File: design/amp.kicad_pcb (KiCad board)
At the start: 2 copper layers, 61 x 36 mm, 57 parts, among them IC1 CP2102N-A02-GQFN24R, IC2 STM6601CQ2BDM6F, IC3 LD39200PU33R, J1 USB4105-GF-A, J2 SM04B-SRSS-TB(LF)(SN), J3 SM04B-SRSS-TB(LF)(SN), J4 Conn_01x02_Female, J5 Conn_02x03_Odd_Even, J6 SM04B-SRSS-TB(LF)(SN), J7 SM04B-SRSS-TB(LF)(SN), Q1 PMBT2222,215, Q2 PMBT2222,215, Q3 Si2347DS-T1-GE3, U1 ESP32-WROOM-32D, U2 LIS2HH12

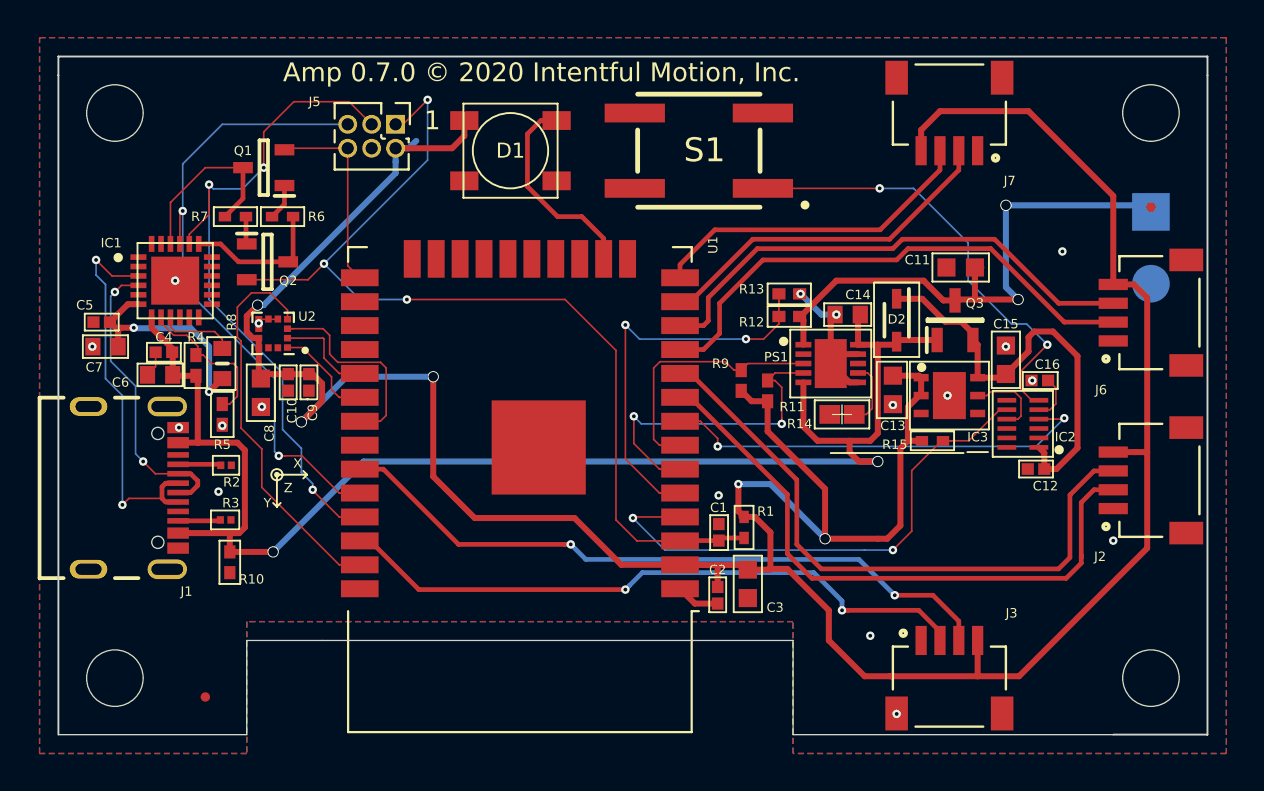
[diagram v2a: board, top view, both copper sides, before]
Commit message: added silkscreen logo to the front
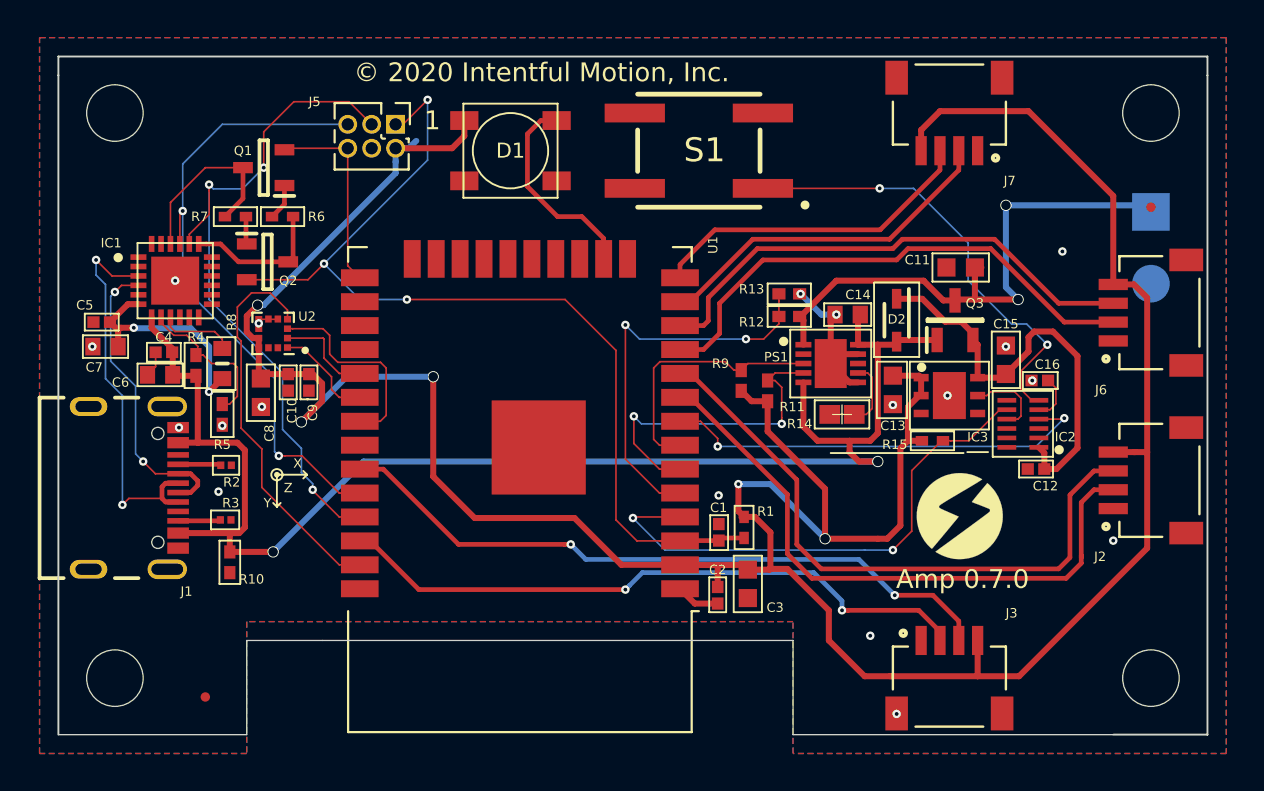
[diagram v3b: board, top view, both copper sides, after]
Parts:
- added G***: LOGO, amp:amp-logo, F.Cu at (102.8, 56.4)
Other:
- board text added: "Amp 0.7.0"
- board text added: "© 2020 Intentful Motion, Inc."
- board text removed: "Amp 0.7.0 © 2020 Intentful Motion, Inc."
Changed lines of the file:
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@@
   (general
     (thickness 1.6)
-    (drawings 166)
+    (drawings 167)
     (tracks 568)
     (zones 0)
-    (modules 57)
+    (modules 58)
     (nets 43)
   )
@@
     (add_net /VBUS)
     (add_net /V_FILTERED)
+  )
+  (module amp:amp-logo (layer F.Cu)
+    (at 102.85 56.4)
+    (fp_text reference G*** (at 0 0) (layer F.SilkS) hide
+      (effects (font (size 1.524 1.524) (thickness 0.3)))
+    )
+    (fp_text value LOGO (at 0.75 0) (layer F.SilkS) hide
+      (effects (font (size 1.524 1.524) (thickness 0.3)))
+    )
+    (fp_poly (pts (xy 0.339631 -2.2609) (xy 0.611164 -2.204276) (xy 0.651933 -2.192876) (xy 0.716583 -2.171689)
+      (xy 0.79467 -2.142301) (xy 0.879853 -2.10755) (xy 0.965792 -2.070276) (xy 1.046146 -2.033319)
+      (xy 1.114576 -1.999519) (xy 1.164739 -1.971716) (xy 1.190296 -1.952749) (xy 1.191363 -1.951276)
+      (xy 1.178872 -1.940034) (xy 1.139122 -1.912971) (xy 1.07412 -1.871311) (xy 0.985873 -1.816277)
+      (xy 0.876386 -1.749093) (xy 0.747666 -1.670983) (xy 0.601719 -1.58317) (xy 0.440552 -1.486878)
+      (xy 0.266171 -1.383331) (xy 0.080581 -1.273753) (xy 0.080299 -1.273587) (xy -0.13535 -1.146559)
+      (xy -0.323594 -1.035441) (xy -0.486231 -0.938991) (xy -0.625055 -0.855963) (xy -0.741864 -0.785113)
+      (xy -0.838453 -0.725198) (xy -0.916619 -0.674973) (xy -0.978156 -0.633193) (xy -1.024863 -0.598614)
+      (xy -1.058533 -0.569993) (xy -1.080964 -0.546084) (xy -1.093952 -0.525644) (xy -1.099292 -0.507428)
+      (xy -1.098781 -0.490191) (xy -1.094215 -0.472691) (xy -1.090593 -0.462414) (xy -1.082006 -0.448774)
+      (xy -1.063741 -0.432893) (xy -1.032754 -0.413239) (xy -0.986004 -0.388281) (xy -0.920448 -0.356486)
+      (xy -0.833044 -0.316323) (xy -0.720748 -0.266262) (xy -0.580519 -0.204769) (xy -0.567267 -0.19899)
+      (xy -0.444872 -0.145565) (xy -0.332721 -0.096501) (xy -0.234507 -0.053419) (xy -0.15392 -0.017944)
+      (xy -0.094652 0.008301) (xy -0.060395 0.023691) (xy -0.053305 0.027091) (xy -0.063057 0.040216)
+      (xy -0.092351 0.076682) (xy -0.138999 0.133857) (xy -0.200808 0.209107) (xy -0.275591 0.299801)
+      (xy -0.361156 0.403305) (xy -0.455314 0.516986) (xy -0.555875 0.638212) (xy -0.660649 0.764351)
+      (xy -0.767446 0.892768) (xy -0.874077 1.020832) (xy -0.97835 1.14591) (xy -1.078077 1.265369)
+      (xy -1.171067 1.376576) (xy -1.25513 1.476899) (xy -1.328077 1.563705) (xy -1.387717 1.634361)
+      (xy -1.431861 1.686234) (xy -1.458318 1.716691) (xy -1.462855 1.721659) (xy -1.481062 1.727669)
+      (xy -1.510155 1.712924) (xy -1.550699 1.679325) (xy -1.735413 1.490653) (xy -1.894487 1.282266)
+      (xy -2.027305 1.057265) (xy -2.133251 0.818754) (xy -2.21171 0.569834) (xy -2.262067 0.313609)
+      (xy -2.283706 0.053182) (xy -2.276012 -0.208346) (xy -2.23837 -0.467871) (xy -2.170163 -0.722292)
+      (xy -2.074379 -0.960928) (xy -1.94076 -1.2056) (xy -1.783029 -1.428111) (xy -1.603501 -1.627416)
+      (xy -1.404491 -1.802469) (xy -1.188314 -1.952223) (xy -0.957284 -2.075632) (xy -0.713717 -2.171651)
+      (xy -0.459927 -2.239234) (xy -0.198229 -2.277333) (xy 0.069062 -2.284904) (xy 0.339631 -2.2609)) (layer F.SilkS) (width 0.01))
+    (fp_poly (pts (xy 1.532466 -1.6969) (xy 1.619901 -1.612815) (xy 1.7144 -1.509411) (xy 1.806976 -1.397193)
+      (xy 1.888648 -1.286667) (xy 1.908464 -1.257261) (xy 2.045847 -1.019103) (xy 2.151693 -0.772899)
+      (xy 2.226682 -0.52104) (xy 2.271496 -0.265921) (xy 2.286814 -0.009933) (xy 2.273318 0.24453)
+      (xy 2.231688 0.495076) (xy 2.162603 0.739311) (xy 2.066746 0.974843) (xy 1.944797 1.199279)
+      (xy 1.797435 1.410226) (xy 1.625342 1.605292) (xy 1.429198 1.782082) (xy 1.209684 1.938205)
+      (xy 0.96748 2.071267) (xy 0.960927 2.074378) (xy 0.72968 2.166412) (xy 0.482209 2.233065)
+      (xy 0.225847 2.273288) (xy -0.032076 2.286033) (xy -0.284225 2.270251) (xy -0.347134 2.261471)
+      (xy -0.610327 2.203274) (xy -0.869288 2.111799) (xy -1.007534 2.048393) (xy -1.086669 2.008267)
+      (xy -1.157757 1.970718) (xy -1.213676 1.939613) (xy -1.247304 1.918815) (xy -1.249989 1.916819)
+      (xy -1.289245 1.886177) (xy 0.143025 0.839913) (xy 0.338995 0.696569) (xy 0.527379 0.558406)
+      (xy 0.706354 0.42678) (xy 0.874099 0.303047) (xy 1.028792 0.188565) (xy 1.168609 0.084689)
+      (xy 1.291728 -0.007224) (xy 1.396327 -0.085817) (xy 1.480584 -0.149733) (xy 1.542677 -0.197617)
+      (xy 1.580782 -0.228112) (xy 1.592995 -0.239425) (xy 1.604256 -0.280283) (xy 1.605447 -0.324777)
+      (xy 1.603293 -0.339943) (xy 1.597912 -0.353342) (xy 1.585922 -0.366645) (xy 1.563943 -0.381524)
+      (xy 1.528594 -0.399651) (xy 1.476494 -0.422698) (xy 1.404263 -0.452336) (xy 1.308519 -0.490237)
+      (xy 1.185882 -0.538074) (xy 1.13087 -0.55946) (xy 1.011783 -0.605715) (xy 0.902664 -0.648044)
+      (xy 0.807581 -0.684875) (xy 0.730599 -0.714633) (xy 0.675784 -0.735747) (xy 0.647203 -0.746642)
+      (xy 0.644304 -0.747699) (xy 0.650926 -0.761494) (xy 0.677173 -0.79833) (xy 0.720809 -0.855383)
+      (xy 0.779599 -0.929829) (xy 0.851306 -1.018844) (xy 0.933694 -1.119603) (xy 1.024526 -1.229284)
+      (xy 1.0459 -1.254904) (xy 1.464733 -1.756274) (xy 1.532466 -1.6969)) (layer F.SilkS) (width 0.01))
   )
   (module SamacSys_Parts:RESC1005X40N (layer F.Cu)
@@
     )
   )
+  (gr_text "Amp 0.7.0" (at 103 59.75) (layer F.SilkS)
+    (effects (font (size 1 1) (thickness 0.25)))
+  )
   (gr_text + (at 110.3 40.05) (layer B.SilkS)
     (effects (font (size 2 2) (thickness 0.25)) (justify mirror))
@@
   (gr_line (start 92.35 61.5) (end 92.35 58.5) (layer F.SilkS) (width 0.1))
   (gr_line (start 90.85 61.5) (end 92.35 61.5) (layer F.SilkS) (width 0.1))
-  (gr_text "Amp 0.7.0 © 2020 Intentful Motion, Inc." (at 80.65 32.85) (layer F.SilkS)
+  (gr_text "© 2020 Intentful Motion, Inc." (at 80.65 32.85) (layer F.SilkS)
     (effects (font (size 1 1) (thickness 0.2)))
   )

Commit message: Swapped out DIO5158 for MCP83733 (part shortage)
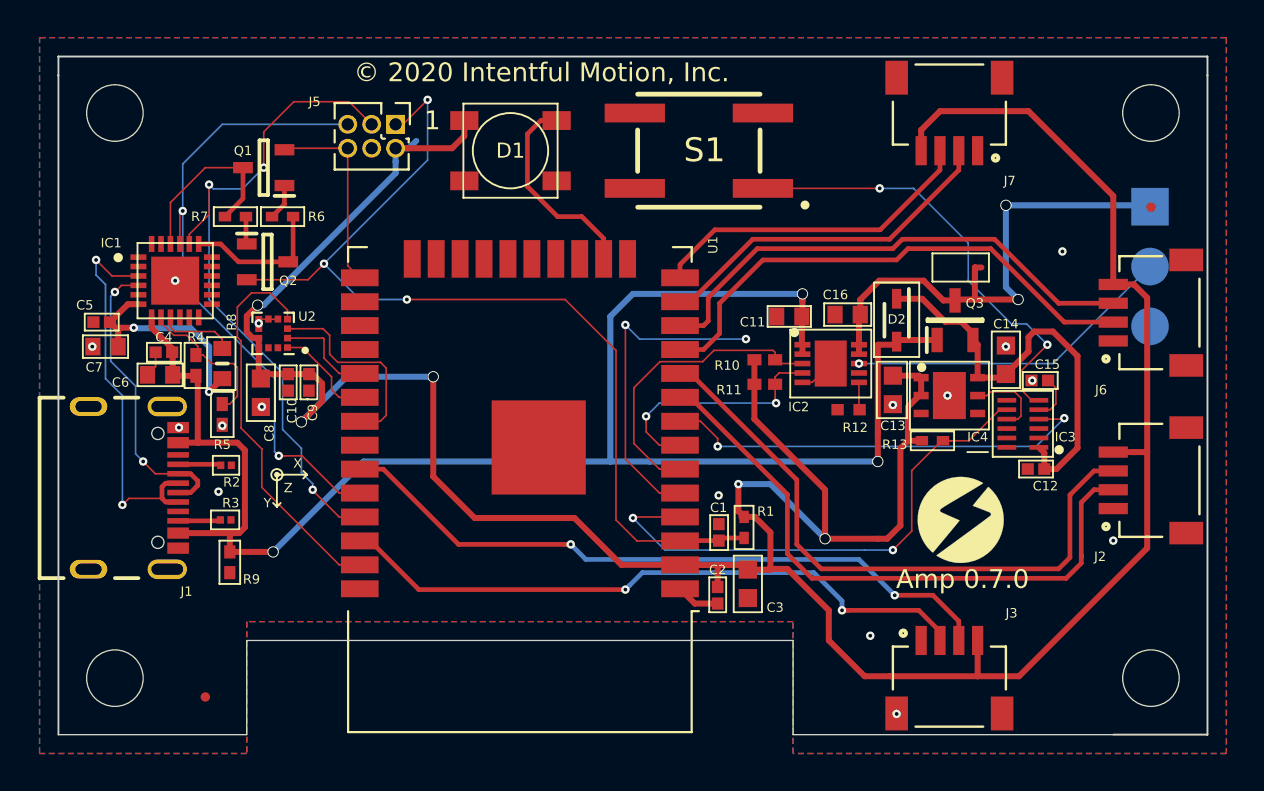
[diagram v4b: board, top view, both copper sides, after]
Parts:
- removed the C11 at (102.9, 43.2)
- removed PS1: DIO5158CD10, SamacSys_Parts:SON50P300X300X80-11N-D
- removed the R13 at (93.8, 44.6)
- removed R14: RC0603FR-101K2L, SamacSys_Parts:RESC1608X55N
- added C16: TMK107BJ105KA-T, SamacSys_Parts:CAPC1608X90N, F.Cu at (96.9, 45.7)
- added IC2: MCP73833-FCI_MF, SamacSys_Parts:SON50P300X300X100-11N-D, F.Cu at (96.0, 48.3)
- J4: value Conn_01x02_Female -> Conn_01x03_Female; footprint Connector_Wire:SolderWirePad_1x02_P3.81mm_Drill0.8mm -> Connector_Wire:SolderWirePad_1x03_P3.175mm_Drill0.8mm
- R12: value AC0402FR-13100KL -> RR0510P-102-D; footprint SamacSys_Parts:RESC1005X37N -> SamacSys_Parts:RESC1005X40N
- R4: value CRCW0402140RFKEDC -> CRCW040222K6FKEDC
- moved R12 5.87 mm to (97.0, 50.8), turned to 180 degrees
- moved G*** 3.21 mm to (72.4, 50.4)
- moved C11 3.10 mm to (93.8, 45.8), turned to 0 degrees
- moved R11 1.66 mm to (92.5, 48.1), turned to 0 degrees
- moved R10 1.27 mm to (92.5, 49.4), turned to 0 degrees
- moved J4 0.28 mm to (113.0, 40.0)
- moved G*** 0.21 mm to (102.9, 56.6)
- renumbered C14 to C11, C15 to C14, C16 to C15, IC2 to IC3, IC3 to IC4, R9 to R10, R15 to R13, R10 to R9
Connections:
- net /CHRG renamed /CHARGE
- C11 pad 1: /VBUS -> GND
- C11 pad 2: GND -> /VBUS
- J4 pad 2: GND -> /BAT_TEMP
- R12 pad 1: /VBAT_SENSE -> Net-(IC2-Pad6)
- R12 pad 2: /VBAT -> GND
- U1 pad 5: /VBAT_SENSE -> (no net)
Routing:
- net /VBAT_SENSE: track 21.1 -> 0.00 mm, vias 2 -> 0
- net /BAT_TEMP: track 0.00 -> 17.6 mm, vias 0 -> 1
- net (no net): track 0.00 -> 17.5 mm, vias 0 -> 2
- net /VBUS: track 77.8 -> 89.5 mm, vias 2 -> 3
- net GND: track 13.8 -> 7.16 mm, vias 18 -> 16
- net Net-(PS1-Pad7): track 3.58 -> 0.00 mm
- net /VBAT: track 30.3 -> 28.0 mm
- net Net-(IC2-Pad6): track 0.00 -> 1.46 mm
- net /CHARGE: track 17.4 -> 16.3 mm, vias 2 -> 0
- net +3V3: track 164.1 -> 165.0 mm
- net /DONE: track 13.7 -> 13.1 mm, vias 0 -> 2
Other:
- board text added: "-"

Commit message: update board layout
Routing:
- net (no net): track 17.5 -> 0.00 mm, vias 2 -> 0
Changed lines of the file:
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@@
     (thickness 1.6)
     (drawings 159)
-    (tracks 560)
+    (tracks 551)
     (zones 0)
     (modules 56)
@@
     (add_net /TXD0)
     (add_net GND)
-    (add_net "Net-(D1-Pad2)")
-    (add_net "Net-(IC1-Pad1)")
-    (add_net "Net-(IC1-Pad10)")
-    (add_net "Net-(IC1-Pad11)")
-    (add_net "Net-(IC1-Pad12)")
-    (add_net "Net-(IC1-Pad13)")
-    (add_net "Net-(IC1-Pad14)")
-    (add_net "Net-(IC1-Pad15)")
-    (add_net "Net-(IC1-Pad16)")
-    (add_net "Net-(IC1-Pad17)")
-    (add_net "Net-(IC1-Pad18)")
-    (add_net "Net-(IC1-Pad23)")
-    (add_net "Net-(IC1-Pad24)")
-    (add_net "Net-(IC1-Pad5)")
     (add_net "Net-(IC1-Pad8)")
     (add_net "Net-(IC1-Pad9)")
     (add_net "Net-(IC2-Pad6)")
-    (add_net "Net-(IC2-Pad7)")
-    (add_net "Net-(IC3-Pad10)")
-    (add_net "Net-(IC3-Pad11)")
-    (add_net "Net-(IC3-Pad2)")
-    (add_net "Net-(IC3-Pad3)")
-    (add_net "Net-(IC3-Pad7)")
-    (add_net "Net-(IC4-Pad4)")
     (add_net "Net-(J1-PadA5)")
-    (add_net "Net-(J1-PadA8)")
     (add_net "Net-(J1-PadB5)")
-    (add_net "Net-(J1-PadB8)")
     (add_net "Net-(Q1-Pad1)")
     (add_net "Net-(Q2-Pad1)")
-    (add_net "Net-(S1-Pad3)")
-    (add_net "Net-(S1-Pad4)")
-    (add_net "Net-(U1-Pad17)")
-    (add_net "Net-(U1-Pad18)")
-    (add_net "Net-(U1-Pad19)")
-    (add_net "Net-(U1-Pad20)")
-    (add_net "Net-(U1-Pad21)")
-    (add_net "Net-(U1-Pad22)")
-    (add_net "Net-(U1-Pad23)")
-    (add_net "Net-(U1-Pad24)")
-    (add_net "Net-(U1-Pad26)")
-    (add_net "Net-(U1-Pad27)")
-    (add_net "Net-(U1-Pad28)")
-    (add_net "Net-(U1-Pad32)")
-    (add_net "Net-(U2-Pad11)")
-    (add_net "Net-(U2-Pad12)")
   )
   (net_class LEDs ""
@@
   (segment (start 64.9588 41.9088) (end 65 41.95) (width 0.25) (layer F.Cu) (net 14))
   (segment (start 64.9588 40.5) (end 64.9588 41.9088) (width 0.25) (layer F.Cu) (net 14))
-  (via (at 91.5 47) (size 0.45) (drill 0.2) (layers F.Cu B.Cu) (net 0))
-  (segment (start 86.9111 55.175) (end 85.1 53.3639) (width 0.0889) (layer F.Cu) (net 0))
-  (segment (start 88 55.175) (end 86.9111 55.175) (width 0.0889) (layer F.Cu) (net 0))
-  (segment (start 85.1 53.3639) (end 85.1 46.25) (width 0.0889) (layer F.Cu) (net 0))
-  (segment (start 85.1 46.25) (end 85.1 46.25) (width 0.0889) (layer F.Cu) (net 0))
-  (segment (start 85.1 46.25) (end 85.1 46.25) (width 0.0889) (layer F.Cu) (net 0))
-  (via (at 85.1 46.25) (size 0.45) (drill 0.2) (layers F.Cu B.Cu) (net 0))
-  (segment (start 85.85 47) (end 85.1 46.25) (width 0.0889) (layer B.Cu) (net 0))
-  (segment (start 91.5 47) (end 85.85 47) (width 0.0889) (layer B.Cu) (net 0))
   (segment (start 96 48.3139) (end 96 48.3) (width 0.0889) (layer F.Cu) (net 1))
   (segment (start 95.0139 49.3) (end 96 48.3139) (width 0.0889) (layer F.Cu) (net 1))
